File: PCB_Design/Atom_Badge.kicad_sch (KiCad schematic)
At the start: 25 parts

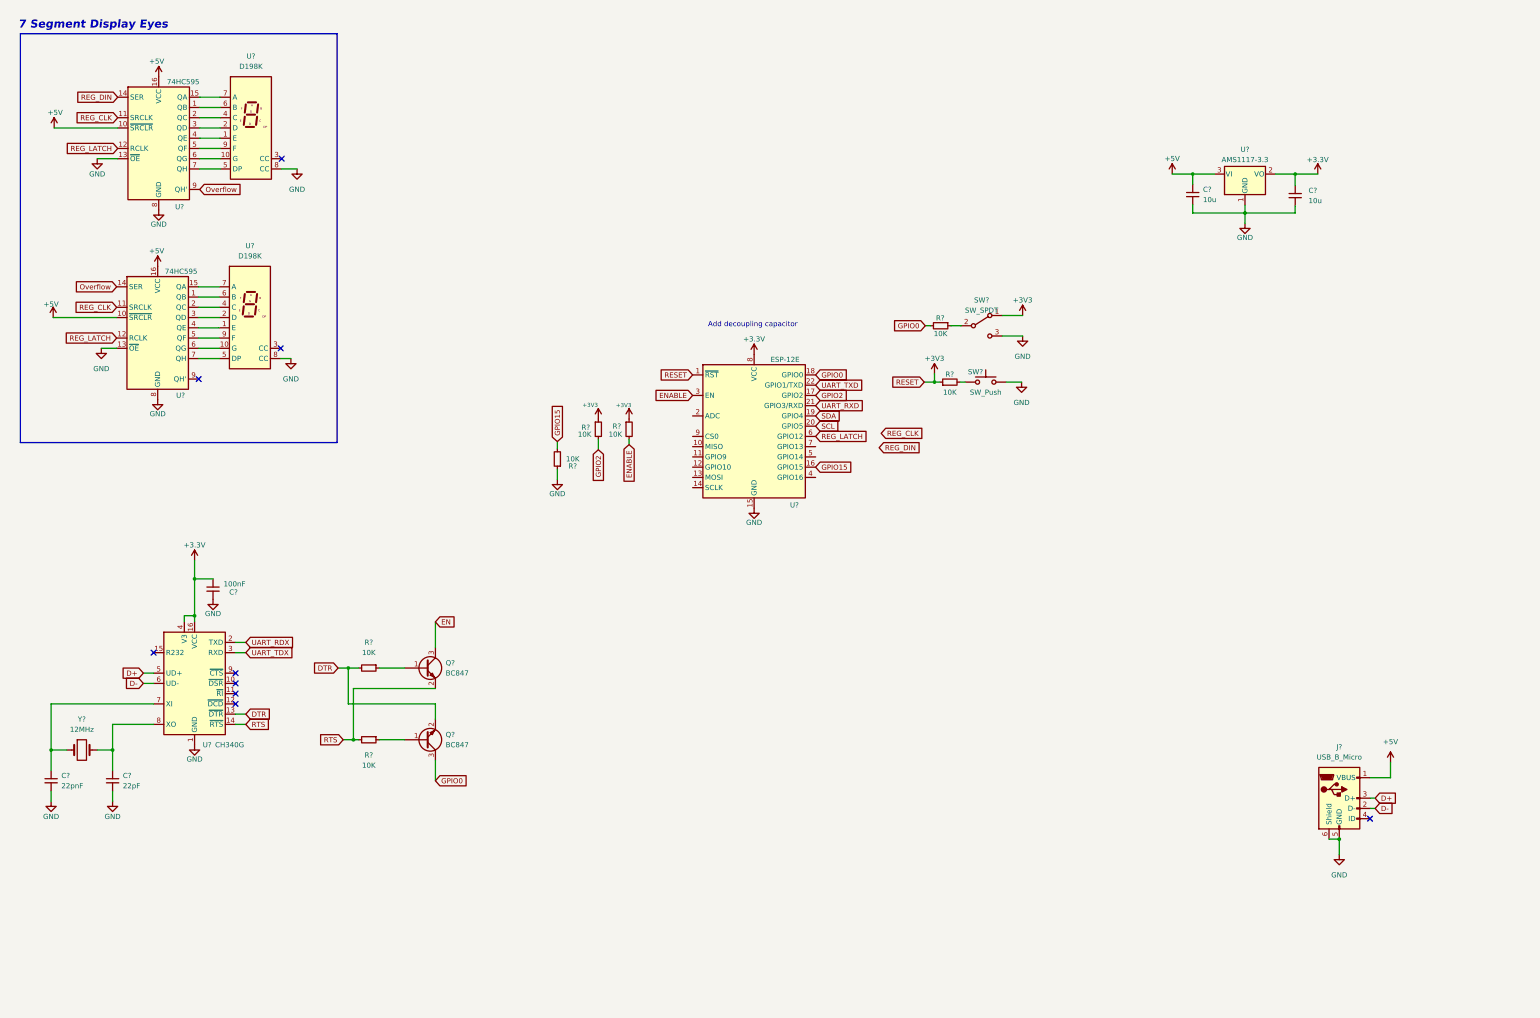
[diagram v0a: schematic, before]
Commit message: Added leds and oled sch
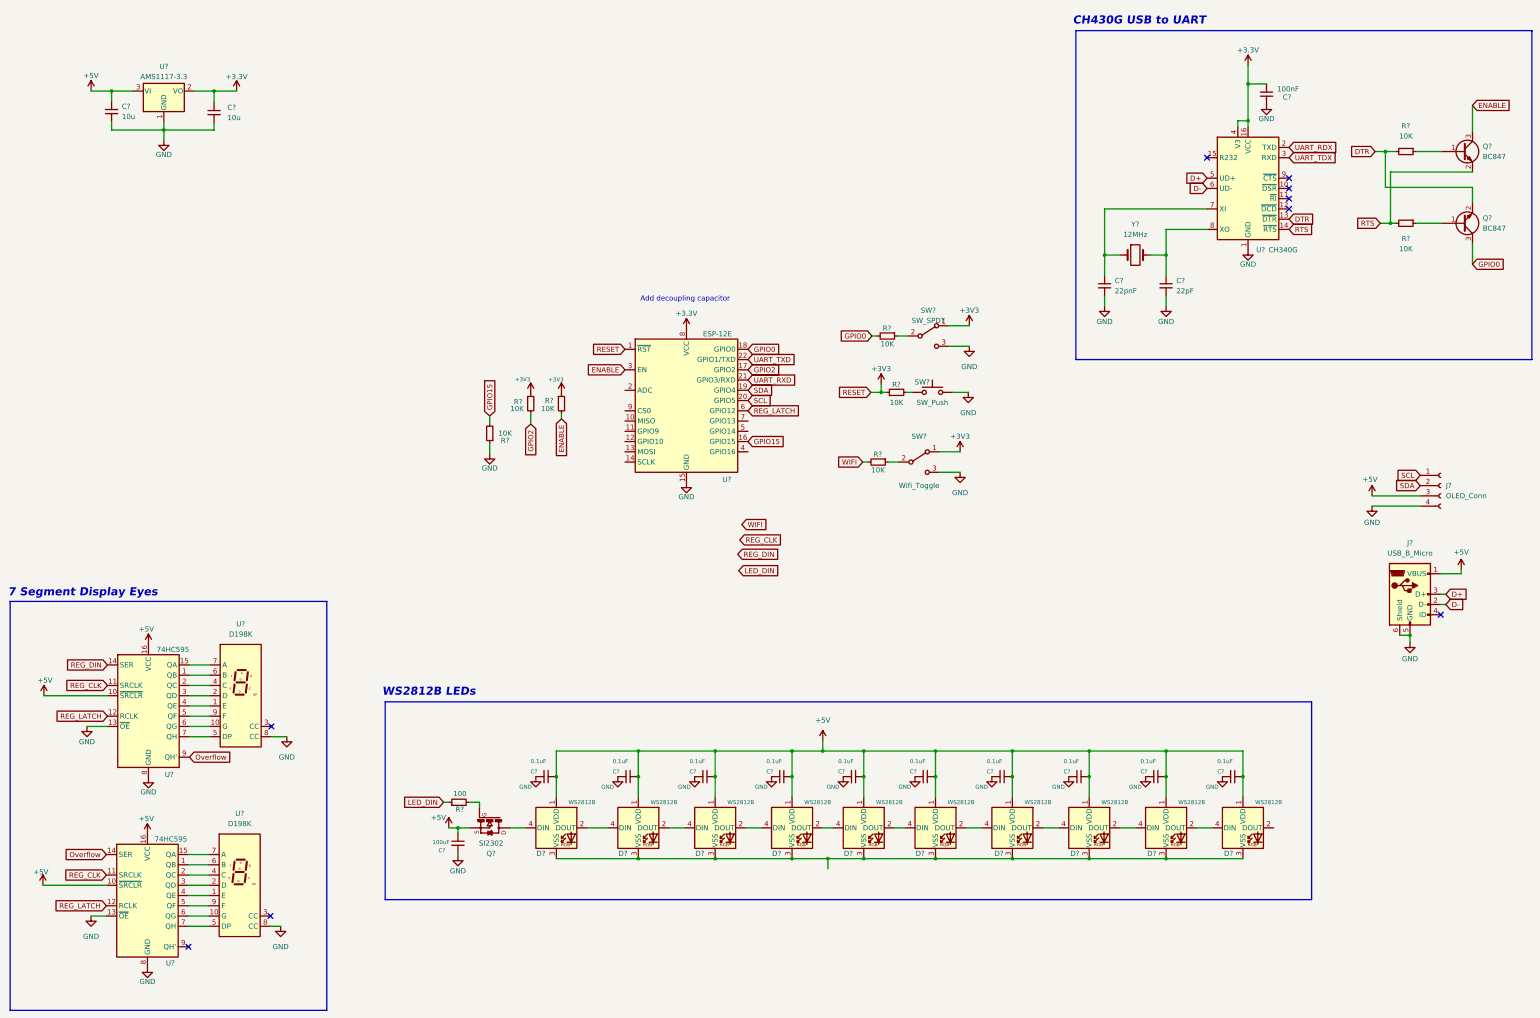
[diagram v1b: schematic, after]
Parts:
- added C? (x10): 0.1uF, Capacitor_SMD:C_1206_3216Metric_Pad1.33x1.80mm_HandSolder, symbol Device:C_Small
- added C?: 100uF, Capacitor_SMD:C_1206_3216Metric_Pad1.33x1.80mm_HandSolder, symbol Device:C_Small
- added D? (x10): WS2812B, LED_SMD:LED_WS2812B_PLCC4_5.0x5.0mm_P3.2mm, symbol LED:WS2812B
- added J?: OLED_Conn, symbol Connector:Conn_01x04_Female
- added Q?: SI2302, Package_TO_SOT_SMD:SOT-23, symbol SI2302:SI2302
- added R?: 10K, Resistor_SMD:R_1206_3216Metric_Pad1.30x1.75mm_HandSolder, symbol Device:R_Small
- added R?: 100, Resistor_SMD:R_1206_3216Metric_Pad1.30x1.75mm_HandSolder, symbol Device:R_Small
- added SW?: Wifi_Toggle, Button_Switch_THT:SW_CuK_OS102011MA1QN1_SPDT_Angled, symbol Switch:SW_SPDT
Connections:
- net EN is gone; now on net ENABLE: Q?.3 (C)
- net +3V3: now also SW?.1 (A)
- net +5V: now also C?.1, C?.1, C?.1, C?.1, C?.1, C?.1, C?.1, C?.1, C?.1, C?.1, C?.1, D?.1 (VDD), D?.1 (VDD), D?.1 (VDD), D?.1 (VDD), D?.1 (VDD), D?.1 (VDD), D?.1 (VDD), D?.1 (VDD), D?.1 (VDD), D?.1 (VDD), J?.3 (Pin_3), Q?.2
- net GND: now also C?.2, C?.2, C?.2, C?.2, C?.2, C?.2, C?.2, C?.2, C?.2, C?.2, C?.2, J?.4 (Pin_4), SW?.3 (C)
- net SCL: now also J?.1 (Pin_1)
- net SDA: now also J?.2 (Pin_2)
- new net: D?.2 (DOUT), D?.4 (DIN) (x9)
- new net: D?.3 (VSS), D?.3 (VSS), D?.3 (VSS), D?.3 (VSS), D?.3 (VSS), D?.3 (VSS), D?.3 (VSS), D?.3 (VSS), D?.3 (VSS), D?.3 (VSS)
- new net: R?.1, SW?.2 (B)
- new net: Q?.1, R?.2
- new net: D?.4 (DIN), Q?.3
- new net LED_DIN: R?.1
- new net WIFI: R?.2
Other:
- note added: "CH430G USB to UART"
- note added: "WS2812B LEDs"
- moved on the sheet: C?, J?, Q?, R?, SW?, U?, Y?

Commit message: new transistor
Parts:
- removed Q? (x2): BC847, Package_TO_SOT_SMD:SOT-23, symbol Transistor_BJT:BC847
- removed R? (x2): 10K, symbol Device:R_Small
- added Q? (x2): S8050, Package_TO_SOT_THT:TO-92_Inline, symbol Transistor_BJT:S8050
- added R? (x2): 10K, symbol Device:R_Small
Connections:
- net DTR: now also Q?.3 (C), R?.2
- net ENABLE: now also Q?.3 (C)
- net GPIO0: now also Q?.1 (E)
- net RTS: now also Q?.1 (E), R?.2
- new net: Q?.2 (B), R?.1 (x2)
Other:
- moved on the sheet: C?, U?, Y?
